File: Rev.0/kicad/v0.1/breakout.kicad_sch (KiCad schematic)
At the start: 29 parts, among them J1 Conn_02x10_Odd_Even, J10 Conn_02x10_Odd_Even, J12 Conn_02x10_Odd_Even, J2 Conn_02x10_Odd_Even, J3 Conn_01x02, J4 Conn_01x03_Pin, J5 Conn_01x05_Pin, U1 RP2040-TINY, U2 PCAL6408APW, U3 PCAL6408APW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

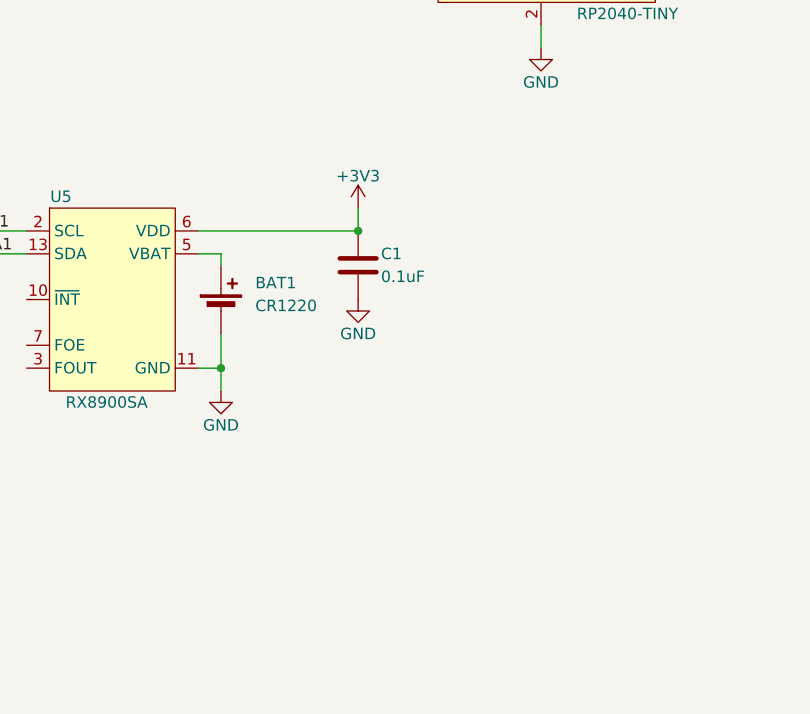
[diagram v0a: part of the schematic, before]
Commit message: Rev 0.1 added backup battery Schottky diodes
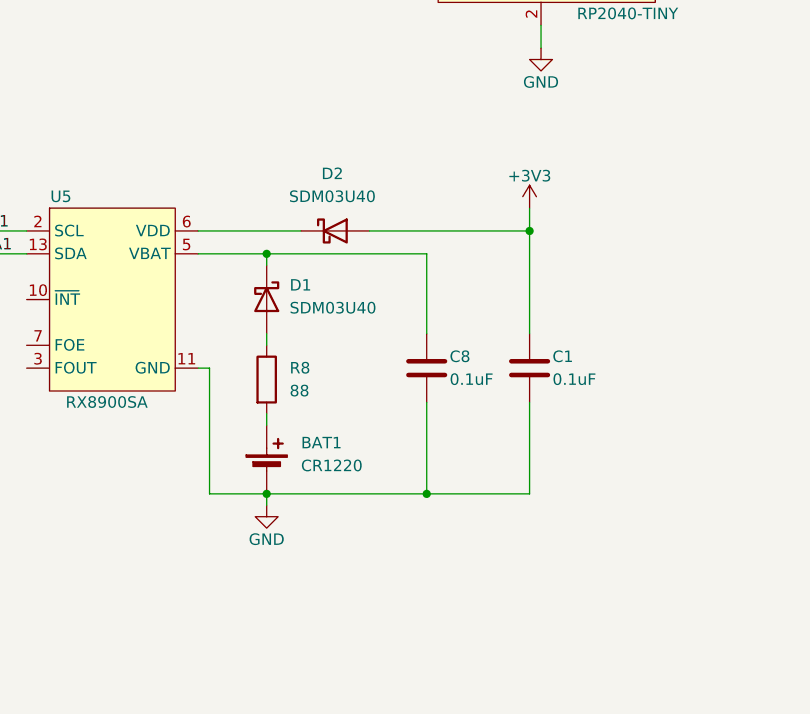
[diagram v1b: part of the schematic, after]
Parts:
- added C8: 0.1uF, Capacitor_SMD:C_0805_2012Metric_Pad1.18x1.45mm_HandSolder, symbol Device:C
- added D1, D2: SDM03U40, Diode_SMD:D_SOD-523, symbol Device:D_Schottky
- added R8: 88, Resistor_SMD:R_1206_3216Metric_Pad1.30x1.75mm_HandSolder, symbol Device:R
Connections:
- net +3V3: now also D2.2 (A); no longer U5.6 (VDD)
- net GND: now also C8.2
- net at U5.5 (VBAT): now also C8.1, D1.1 (K); no longer BAT1.1 (+)
- new net: D1.2 (A), R8.1
- new net: BAT1.1 (+), R8.2
- new net: D2.1 (K), U5.6 (VDD)
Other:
- moved on the sheet: BAT1, C1

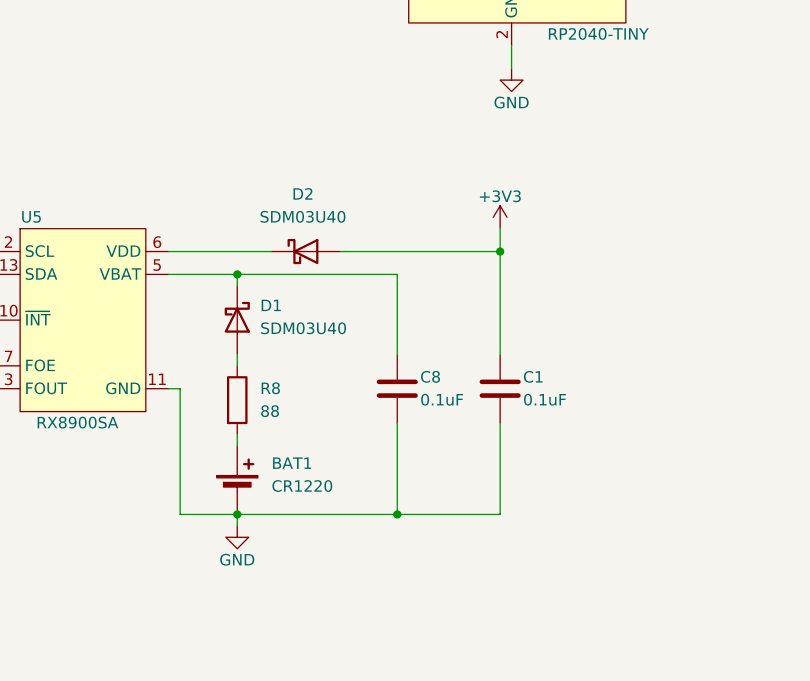
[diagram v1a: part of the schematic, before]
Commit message: Rev 0.1: shuffled decoupling capacitors to correct side of Schottky diodes
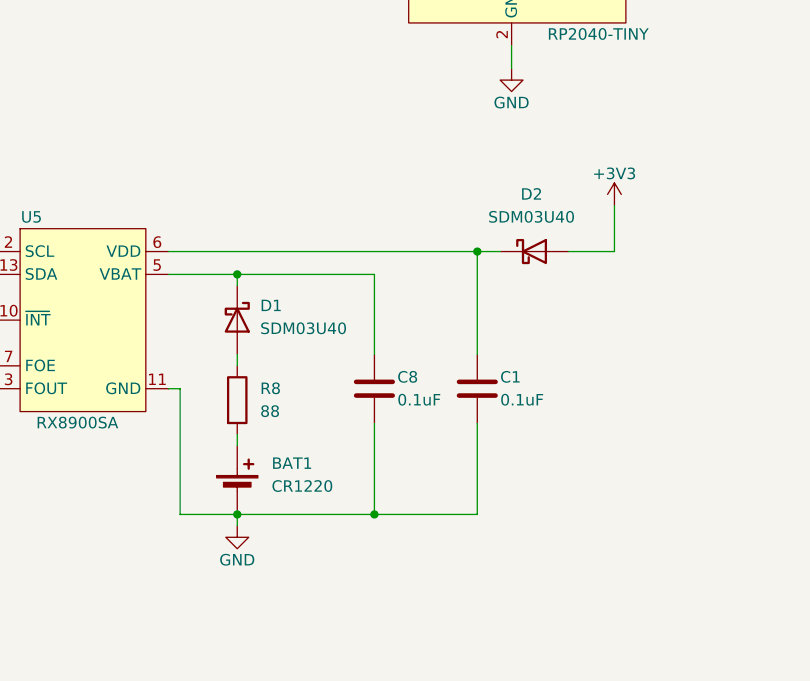
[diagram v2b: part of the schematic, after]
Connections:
- net +3V3: no longer C1.1
- net at D2.1 (K), U5.6 (VDD): now also C1.1
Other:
- moved on the sheet: C1, C8, D2
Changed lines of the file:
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@@
   (junction (at 267.97 41.91) (diameter 0) (color 0 0 0 0)
   )
-  (junction (at 238.76 93.98) (diameter 0) (color 0 0 0 0)
-  )
   (junction (at 160.02 57.15) (diameter 0) (color 0 0 0 0)
   )
@@
   (junction (at 27.94 92.71) (diameter 0) (color 0 0 0 0)
   )
+  (junction (at 236.22 93.98) (diameter 0) (color 0 0 0 0)
+  )
   (junction (at 67.31 24.13) (diameter 0) (color 0 0 0 0)
   )
@@
   (junction (at 205.74 54.61) (diameter 0) (color 0 0 0 0)
   )
+  (junction (at 224.79 123.19) (diameter 0) (color 0 0 0 0)
+  )
   (junction (at 147.32 20.32) (diameter 0) (color 0 0 0 0)
   )
@@
   (junction (at 267.97 57.15) (diameter 0) (color 0 0 0 0)
   )
-  (junction (at 227.33 123.19) (diameter 0) (color 0 0 0 0)
-  )
   (junction (at 73.66 24.13) (diameter 0) (color 0 0 0 0)
   )
@@
     (stroke (width 0) (type default))
   )
-  (bus (pts (xy 115.57 151.13) (xy 115.57 153.67))
+  (wire (pts (xy 236.22 93.98) (xy 238.76 93.98))
     (stroke (width 0) (type default))
   )
-  (wire (pts (xy 238.76 91.44) (xy 238.76 93.98))
+  (bus (pts (xy 115.57 151.13) (xy 115.57 153.67))
     (stroke (width 0) (type default))
   )
@@
     (stroke (width 0) (type default))
   )
-  (wire (pts (xy 238.76 113.03) (xy 238.76 123.19))
+  (wire (pts (xy 236.22 113.03) (xy 236.22 123.19))
     (stroke (width 0) (type default))
   )
@@
     (stroke (width 0) (type default))
   )
-  (wire (pts (xy 238.76 93.98) (xy 238.76 105.41))
-    (stroke (width 0) (type default))
-  )
   (bus (pts (xy 20.32 36.83) (xy 20.32 39.37))
     (stroke (width 0) (type default))
@@
     (stroke (width 0) (type default))
   )
-  (wire (pts (xy 220.98 93.98) (xy 238.76 93.98))
-    (stroke (width 0) (type default))
-  )
   (bus (pts (xy 20.32 82.55) (xy 20.32 87.63))
     (stroke (width 0) (type default))
@@
     (stroke (width 0) (type default))
   )
-  (wire (pts (xy 201.93 93.98) (xy 213.36 93.98))
+  (wire (pts (xy 251.46 93.98) (xy 251.46 88.9))
     (stroke (width 0) (type default))
   )
@@
     (stroke (width 0) (type default))
   )
+  (wire (pts (xy 236.22 93.98) (xy 236.22 105.41))
+    (stroke (width 0) (type default))
+  )
   (bus (pts (xy 109.22 87.63) (xy 109.22 85.09))
     (stroke (width 0) (type default))
@@
     (stroke (width 0) (type default))
   )
+  (wire (pts (xy 224.79 123.19) (xy 236.22 123.19))
+    (stroke (width 0) (type default))
+  )
   (bus (pts (xy 73.66 77.47) (xy 73.66 80.01))
     (stroke (width 0) (type default))
@@
     (stroke (width 0) (type default))
   )
+  (wire (pts (xy 246.38 93.98) (xy 251.46 93.98))
+    (stroke (width 0) (type default))
+  )
   (bus (pts (xy 20.32 34.29) (xy 20.32 31.75))
     (stroke (width 0) (type default))
   )
-  (wire (pts (xy 227.33 105.41) (xy 227.33 96.52))
+  (wire (pts (xy 224.79 105.41) (xy 224.79 96.52))
     (stroke (width 0) (type default))
   )
@@
     (stroke (width 0) (type default))
   )
+  (wire (pts (xy 201.93 93.98) (xy 236.22 93.98))
+    (stroke (width 0) (type default))
+  )
   (bus (pts (xy 115.57 95.25) (xy 115.57 97.79))
     (stroke (width 0) (type default))
@@
     (stroke (width 0) (type default))
   )
-  (wire (pts (xy 238.76 123.19) (xy 227.33 123.19))
-    (stroke (width 0) (type default))
-  )
   (wire (pts (xy 76.2 85.09) (xy 83.82 85.09))
     (stroke (width 0) (type default))
@@
     (stroke (width 0) (type default))
   )
+  (wire (pts (xy 224.79 123.19) (xy 209.55 123.19))
+    (stroke (width 0) (type default))
+  )
   (wire (pts (xy 96.52 52.07) (xy 101.6 52.07))
     (stroke (width 0) (type default))
@@
     (stroke (width 0) (type default))
   )
-  (wire (pts (xy 227.33 113.03) (xy 227.33 123.19))
+  (wire (pts (xy 224.79 113.03) (xy 224.79 123.19))
     (stroke (width 0) (type default))
   )
@@
     (stroke (width 0) (type default))
   )
-  (wire (pts (xy 227.33 123.19) (xy 209.55 123.19))
-    (stroke (width 0) (type default))
-  )
   (wire (pts (xy 49.53 100.33) (xy 64.77 100.33))
     (stroke (width 0) (type default))
@@
     (stroke (width 0) (type default))
   )
-  (wire (pts (xy 227.33 96.52) (xy 209.55 96.52))
+  (wire (pts (xy 224.79 96.52) (xy 209.55 96.52))
     (stroke (width 0) (type default))
   )
@@
     )
   )
-  (symbol (lib_id "Device:C") (at 227.33 109.22 0) (unit 1)
+  (symbol (lib_id "Device:C") (at 224.79 109.22 0) (unit 1)
     (in_bom yes) (on_board yes) (dnp no)
-    (property "Reference" "C8" (at 229.87 107.95 0)
+    (property "Reference" "C8" (at 227.33 107.95 0)
       (effects (font (size 1.27 1.27)) (justify left))
     )
-    (property "Value" "0.1uF" (at 229.87 110.49 0)
+    (property "Value" "0.1uF" (at 227.33 110.49 0)
       (effects (font (size 1.27 1.27)) (justify left))
     )
-    (property "Footprint" "Capacitor_SMD:C_0805_2012Metric_Pad1.18x1.45mm_HandSolder" (at 228.2952 113.03 0)
+    (property "Footprint" "Capacitor_SMD:C_0805_2012Metric_Pad1.18x1.45mm_HandSolder" (at 225.7552 113.03 0)
       (effects (font (size 1.27 1.27)) hide)
     )
-    (property "Datasheet" "~" (at 227.33 109.22 0)
+    (property "Datasheet" "~" (at 224.79 109.22 0)
       (effects (font (size 1.27 1.27)) hide)
     )
@@
     )
   )
-  (symbol (lib_id "Device:D_Schottky") (at 217.17 93.98 0) (unit 1)
+  (symbol (lib_id "Device:D_Schottky") (at 242.57 93.98 0) (unit 1)
     (in_bom yes) (on_board yes) (dnp no) (fields_autoplaced)
-    (property "Reference" "D2" (at 216.8525 87.63 0)
+    (property "Reference" "D2" (at 242.2525 87.63 0)
       (effects (font (size 1.27 1.27)))
     )
-    (property "Value" "SDM03U40" (at 216.8525 90.17 0)
+    (property "Value" "SDM03U40" (at 242.2525 90.17 0)
       (effects (font (size 1.27 1.27)))
     )
-    (property "Footprint" "Diode_SMD:D_SOD-523" (at 217.17 93.98 0)
+    (property "Footprint" "Diode_SMD:D_SOD-523" (at 242.57 93.98 0)
       (effects (font (size 1.27 1.27)) hide)
     )
-    (property "Datasheet" "https://www.diodes.com/assets/Datasheets/SDM03U40.pdf" (at 217.17 93.98 0)
+    (property "Datasheet" "https://www.diodes.com/assets/Datasheets/SDM03U40.pdf" (at 242.57 93.98 0)
       (effects (font (size 1.27 1.27)) hide)
     )
@@
     )
   )
-  (symbol (lib_id "power:+3V3") (at 238.76 91.44 0) (unit 1)
+  (symbol (lib_id "power:+3V3") (at 251.46 88.9 0) (unit 1)
     (in_bom yes) (on_board yes) (dnp no)
-    (property "Reference" "#PWR010" (at 238.76 95.25 0)
+    (property "Reference" "#PWR010" (at 251.46 92.71 0)
       (effects (font (size 1.27 1.27)) hide)
     )
-    (property "Value" "+3V3" (at 238.76 87.884 0)
+    (property "Value" "+3V3" (at 251.46 85.344 0)
       (effects (font (size 1.27 1.27)))
     )
-    (property "Footprint" "" (at 238.76 91.44 0)
+    (property "Footprint" "" (at 251.46 88.9 0)
       (effects (font (size 1.27 1.27)) hide)
     )
-    (property "Datasheet" "" (at 238.76 91.44 0)
+    (property "Datasheet" "" (at 251.46 88.9 0)
       (effects (font (size 1.27 1.27)) hide)
     )
@@
     )
   )
-  (symbol (lib_id "Device:C") (at 238.76 109.22 0) (unit 1)
+  (symbol (lib_id "Device:C") (at 236.22 109.22 0) (unit 1)
     (in_bom yes) (on_board yes) (dnp no)
-    (property "Reference" "C1" (at 241.3 107.95 0)
+    (property "Reference" "C1" (at 238.76 107.95 0)
       (effects (font (size 1.27 1.27)) (justify left))
     )
-    (property "Value" "0.1uF" (at 241.3 110.49 0)
+    (property "Value" "0.1uF" (at 238.76 110.49 0)
       (effects (font (size 1.27 1.27)) (justify left))
     )
-    (property "Footprint" "Capacitor_SMD:C_0805_2012Metric_Pad1.18x1.45mm_HandSolder" (at 239.7252 113.03 0)
+    (property "Footprint" "Capacitor_SMD:C_0805_2012Metric_Pad1.18x1.45mm_HandSolder" (at 237.1852 113.03 0)
       (effects (font (size 1.27 1.27)) hide)
     )
-    (property "Datasheet" "~" (at 238.76 109.22 0)
+    (property "Datasheet" "~" (at 236.22 109.22 0)
       (effects (font (size 1.27 1.27)) hide)
     )

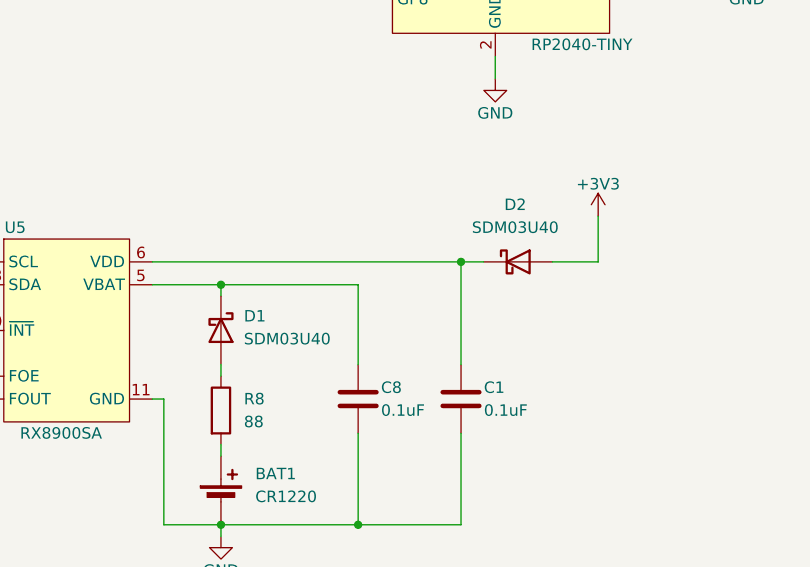
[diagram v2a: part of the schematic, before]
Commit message: Rev 0.1: added RTC battery Schottky diodes
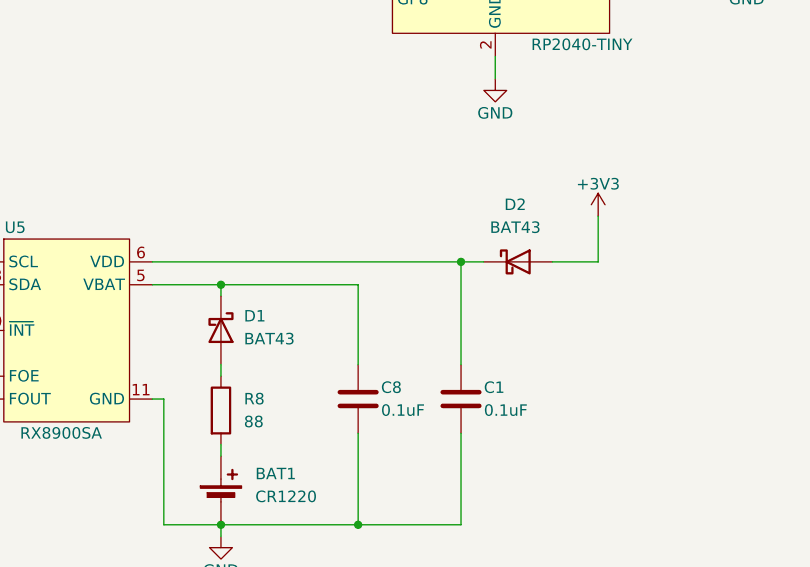
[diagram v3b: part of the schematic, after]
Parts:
- D1, D2: value SDM03U40 -> BAT43; footprint Diode_SMD:D_SOD-523 -> Diode_THT:D_DO-35_SOD27_P7.62mm_Horizontal
- R8: footprint Resistor_SMD:R_1206_3216Metric_Pad1.30x1.75mm_HandSolder -> Resistor_THT:R_Axial_DIN0207_L6.3mm_D2.5mm_P7.62mm_Horizontal
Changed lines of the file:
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@@
       (effects (font (size 1.27 1.27)) (justify left))
     )
-    (property "Value" "SDM03U40" (at 212.09 102.5525 90)
-      (effects (font (size 1.27 1.27)) (justify left))
-    )
-    (property "Footprint" "Diode_SMD:D_SOD-523" (at 209.55 101.6 0)
-      (effects (font (size 1.27 1.27)) hide)
-    )
-    (property "Datasheet" "https://www.diodes.com/assets/Datasheets/SDM03U40.pdf" (at 209.55 101.6 0)
+    (property "Value" "BAT43" (at 212.09 102.5525 90)
+      (effects (font (size 1.27 1.27)) (justify left))
+    )
+    (property "Footprint" "Diode_THT:D_DO-35_SOD27_P7.62mm_Horizontal" (at 209.55 101.6 0)
+      (effects (font (size 1.27 1.27)) hide)
+    )
+    (property "Datasheet" "https://www.vishay.com/docs/85660/bat42.pdf" (at 209.55 101.6 0)
       (effects (font (size 1.27 1.27)) hide)
     )
@@
       (effects (font (size 1.27 1.27)) (justify left))
     )
-    (property "Footprint" "Resistor_SMD:R_1206_3216Metric_Pad1.30x1.75mm_HandSolder" (at 207.772 110.49 90)
+    (property "Footprint" "Resistor_THT:R_Axial_DIN0207_L6.3mm_D2.5mm_P7.62mm_Horizontal" (at 207.772 110.49 90)
       (effects (font (size 1.27 1.27)) hide)
     )
@@
       (effects (font (size 1.27 1.27)))
     )
-    (property "Value" "SDM03U40" (at 242.2525 90.17 0)
-      (effects (font (size 1.27 1.27)))
-    )
-    (property "Footprint" "Diode_SMD:D_SOD-523" (at 242.57 93.98 0)
-      (effects (font (size 1.27 1.27)) hide)
-    )
-    (property "Datasheet" "https://www.diodes.com/assets/Datasheets/SDM03U40.pdf" (at 242.57 93.98 0)
-      (effects (font (size 1.27 1.27)) hide)
-    )
+    (property "Value" "BAT43" (at 242.2525 90.17 0)
+      (effects (font (size 1.27 1.27)))
+    )
+    (property "Footprint" "Diode_THT:D_DO-35_SOD27_P7.62mm_Horizontal" (at 242.57 93.98 0)
+      (effects (font (size 1.27 1.27)) hide)
+    )
+    (property "Datasheet" "https://www.vishay.com/docs/85660/bat42.pdf" (at 242.57 93.98 0)
+      (effects (font (size 1.27 1.27)) hide)
+    )

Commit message: Added RX8900SA battery diodes and resistors to flip side of PCB
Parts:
- D1, D2: footprint Diode_THT:D_DO-35_SOD27_P7.62mm_Horizontal -> Diode_SMD:D_SOD-123
- R8: footprint Resistor_THT:R_Axial_DIN0207_L6.3mm_D2.5mm_P7.62mm_Horizontal -> Resistor_SMD:R_1206_3216Metric_Pad1.30x1.75mm_HandSolder
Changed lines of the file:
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@@
       (effects (font (size 1.27 1.27)) (justify left))
     )
-    (property "Footprint" "Diode_THT:D_DO-35_SOD27_P7.62mm_Horizontal" (at 209.55 101.6 0)
+    (property "Footprint" "Diode_SMD:D_SOD-123" (at 209.55 101.6 0)
       (effects (font (size 1.27 1.27)) hide)
     )
@@
       (effects (font (size 1.27 1.27)) (justify left))
     )
-    (property "Footprint" "Resistor_THT:R_Axial_DIN0207_L6.3mm_D2.5mm_P7.62mm_Horizontal" (at 207.772 110.49 90)
+    (property "Footprint" "Resistor_SMD:R_1206_3216Metric_Pad1.30x1.75mm_HandSolder" (at 207.772 110.49 90)
       (effects (font (size 1.27 1.27)) hide)
     )
@@
       (effects (font (size 1.27 1.27)))
     )
-    (property "Footprint" "Diode_THT:D_DO-35_SOD27_P7.62mm_Horizontal" (at 242.57 93.98 0)
-      (effects (font (size 1.27 1.27)) hide)
-    )
+    (property "Footprint" "Diode_SMD:D_SOD-123" (at 242.57 93.98 0)
+      (effects (font (size 1.27 1.27)) hide)
+    )
